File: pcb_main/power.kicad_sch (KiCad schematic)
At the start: 15 parts, among them U201 MC78L05, U202 MC79L05

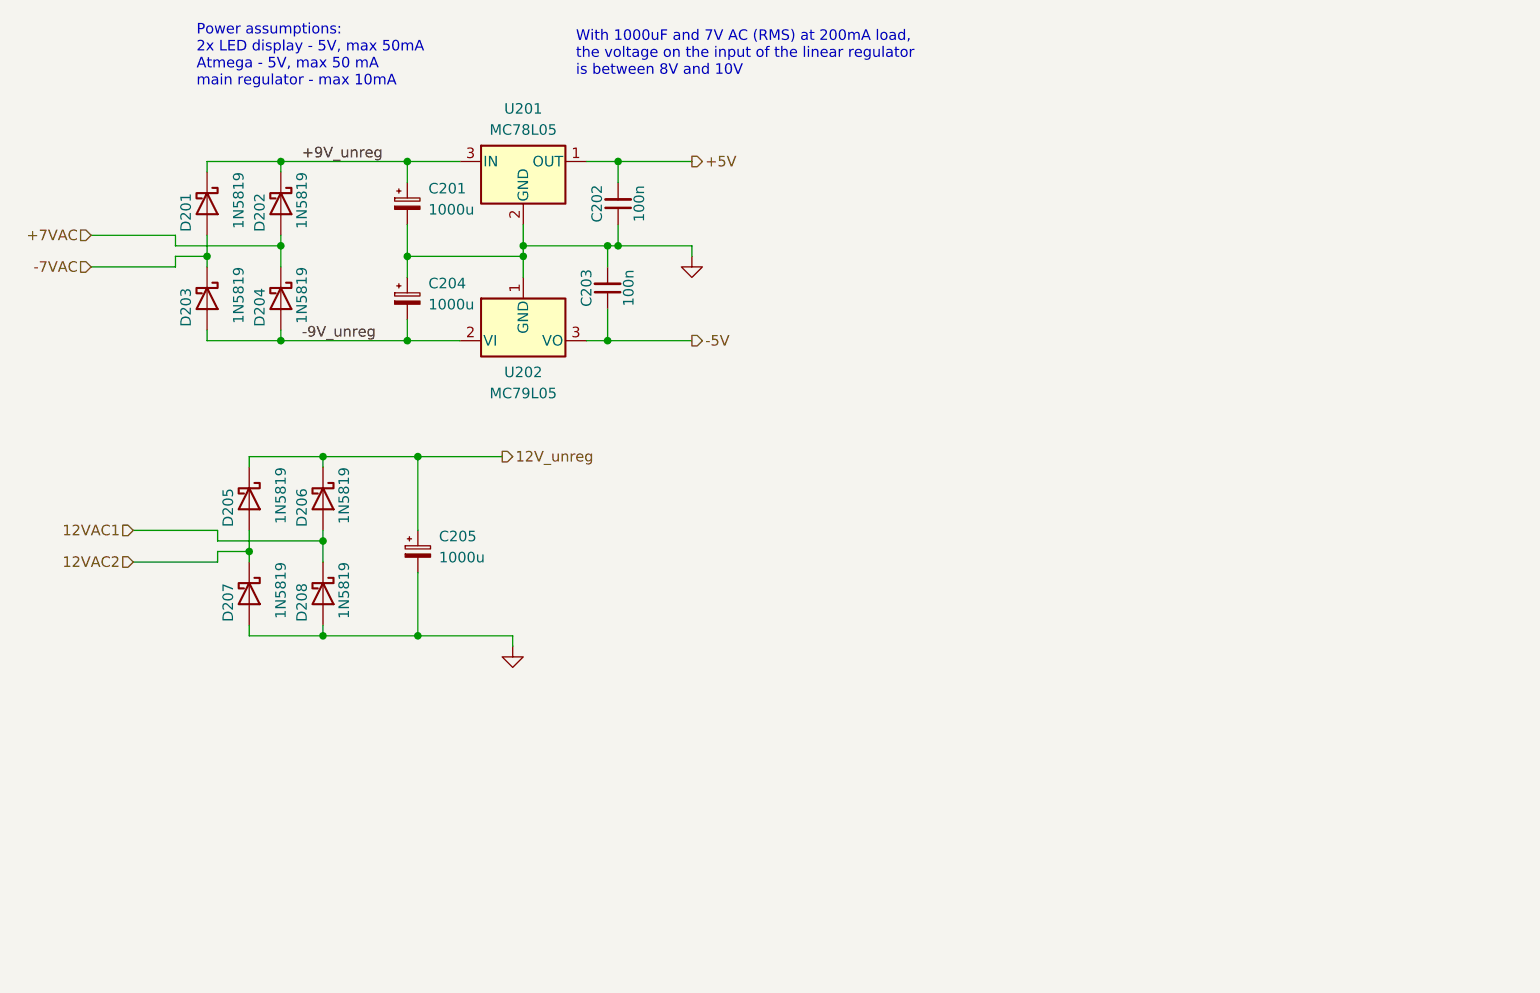
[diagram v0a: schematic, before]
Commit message: power tracks routed
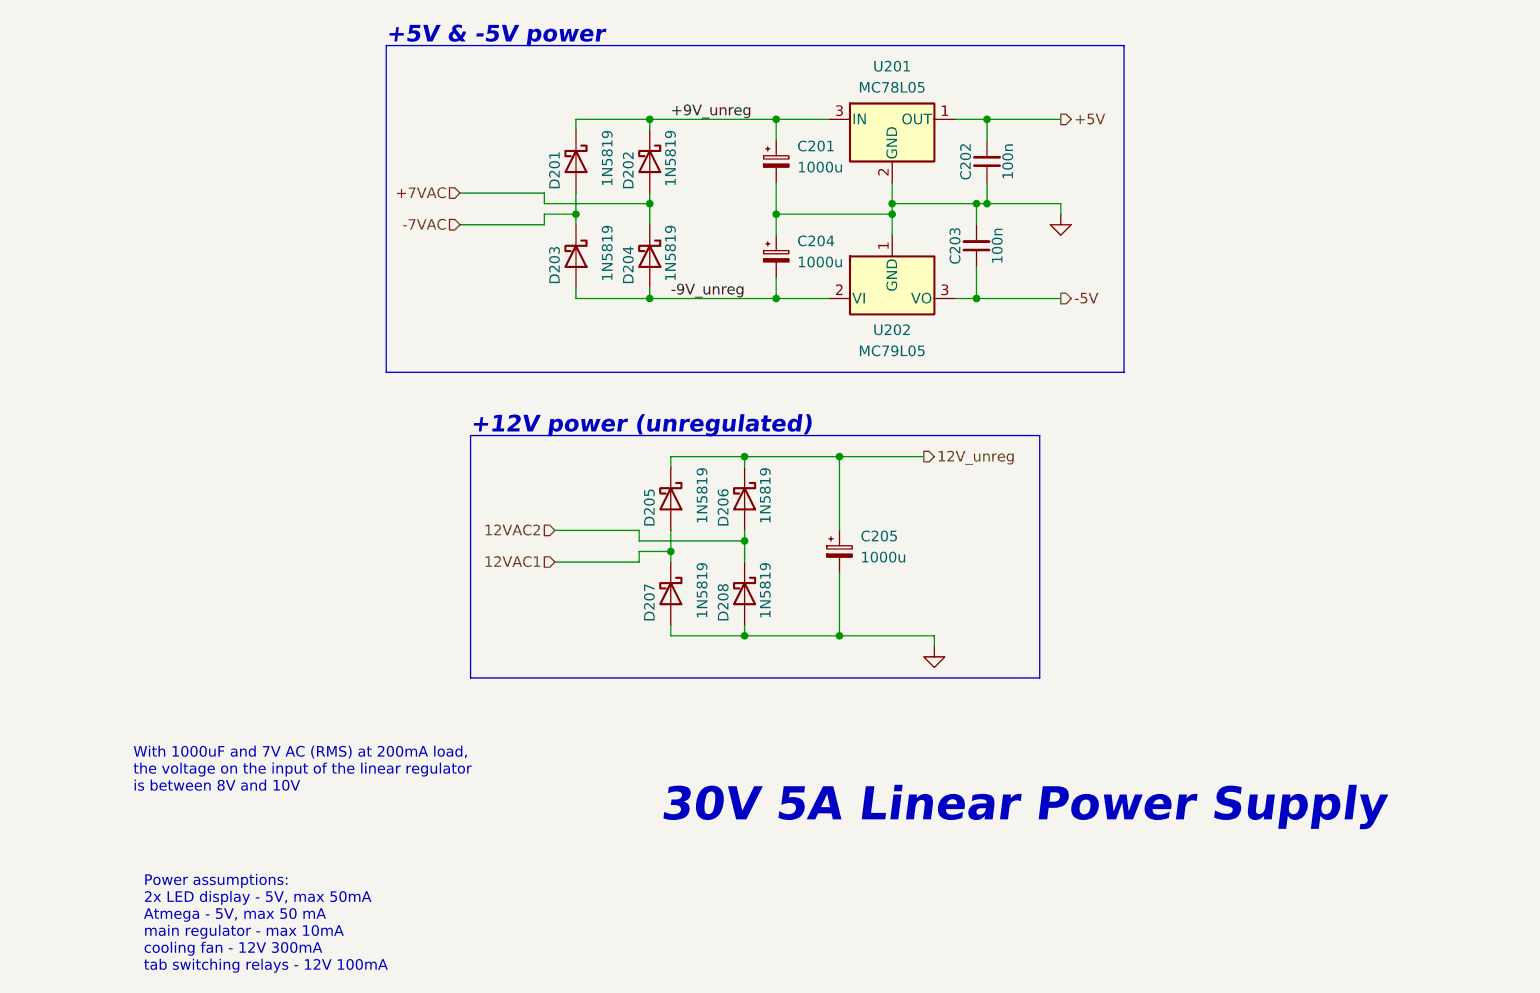
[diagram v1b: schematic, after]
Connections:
- net 12VAC1: now also D205.2 (A), D207.1 (K); no longer D206.2 (A), D208.1 (K)
- net 12VAC2: now also D206.2 (A), D208.1 (K); no longer D205.2 (A), D207.1 (K)
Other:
- note added: "+12V power (unregulated)"
- note added: "+5V & -5V power"
- note added: "30V 5A Linear Power Supply"
- note added: "Power assumptions: 2x LED display - 5V, max 50mA Atmega - 5V, max 50 mA main regulator - max 10mA cooling fan - 12V 300mA tab switching relays - 12V 100mA"
- note removed: "Power assumptions: 2x LED display - 5V, max 50mA Atmega - 5V, max 50 mA main regulator - max 10mA"
- company: (none) -> Dominik Workshop
- title: (none) -> Power section
- moved on the sheet: C201, C202, C203, C204, C205, D201, D202, D203, D204, D205, D206, D207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
